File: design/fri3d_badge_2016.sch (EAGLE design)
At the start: 40 parts, among them Q1 MOSFET-NCHANNEL2N7002PW, U1 MCP73831, Y1 8MHz

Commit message: layout tweaks -> v2
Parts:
- removed J1: (no value), SparkFun-Connectors:USB-AB
- removed J2: (no value), SparkFun-Connectors:JST_2MM_MALE
- removed Y1: 8MHz, SparkFun-FreqCtrl:CRYSTALTXC-7A
- added J3: (no value), SparkFun-Connectors:M02JST-PTH-VERT
- added K1: 65100516121, Input-Output_Connectors_rev15d:65100516121
- added Q2: (no value), crystal:CRYSTALHC49S
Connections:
- net GND: now also J3.1, K1.5GND, K1.GND@1, K1.GND@2; no longer J1.GND, J1.SHIELD, J2.-
- net N$1: now also K1.2D-; no longer J1.D-
- net N$2: now also K1.3D+; no longer J1.D+
- net N$8: now also Q2.2; no longer Y1.2
- net N$9: now also Q2.1; no longer Y1.1
- net USBVCC: now also K1.1VCC; no longer J1.VBUS
- net VCC: now also J3.2; no longer J2.+
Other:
- moved on the sheet: R1, R2
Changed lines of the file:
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@@
 </classes>
 <parts>
-<part name="J1" library="SparkFun-Connectors" deviceset="USB-AB" device=""/>
 <part name="FRAME2" library="SparkFun-Aesthetics" deviceset="FRAME-A4L" device=""/>
 <part name="U$1" library="SparkFun-DigitalIC" deviceset="ATMEGA32U4" device="TQFP-44"/>
@@
 <part name="R3" library="SparkFun-Passives" deviceset="RESISTOR" device="0805-RES" value="10K"/>
 <part name="C1" library="SparkFun-Capacitors" deviceset="CAP" device="0805" value="4.7uF"/>
-<part name="J2" library="SparkFun-Connectors" deviceset="JST_2MM_MALE" device=""/>
 <part name="GND3" library="SparkFun-Aesthetics" deviceset="GND" device=""/>
 <part name="GND4" library="SparkFun-Aesthetics" deviceset="GND" device=""/>
@@
 <part name="GND6" library="SparkFun-Aesthetics" deviceset="GND" device=""/>
 <part name="GND7" library="SparkFun-Aesthetics" deviceset="GND" device=""/>
-<part name="Y1" library="SparkFun-FreqCtrl" deviceset="CRYSTAL" device="TXC-7A" value="8MHz"/>
 <part name="C5" library="SparkFun-Capacitors" deviceset="CAP" device="0805" value="18pF"/>
 <part name="C6" library="SparkFun-Capacitors" deviceset="CAP" device="0805" value="18pF"/>
@@
 <part name="LED3" library="led" deviceset="LED" device="CHIPLED_0805"/>
 <part name="LED4" library="led" deviceset="LED" device="CHIPLED_0805"/>
+<part name="Q2" library="crystal" deviceset="CRYSTAL" device="HC49S"/>
+<part name="J3" library="SparkFun-Connectors" deviceset="M02" device="JST-PTH-VERT"/>
+<part name="K1" library="Input-Output_Connectors_rev15d" deviceset="65100516121" device=""/>
 </parts>
 <sheets>
@@
 </plain>
 <instances>
-<instance part="J1" gate="G$1" x="-30.48" y="134.62" rot="R180"/>
 <instance part="FRAME2" gate="G$1" x="-45.72" y="-7.62"/>
 <instance part="U$1" gate="G$1" x="88.9" y="109.22"/>
-<instance part="R1" gate="G$1" x="-5.08" y="132.08"/>
-<instance part="R2" gate="G$1" x="-5.08" y="139.7"/>
-<instance part="GND1" gate="1" x="-20.32" y="121.92"/>
+<instance part="R1" gate="G$1" x="7.62" y="139.7"/>
+<instance part="R2" gate="G$1" x="7.62" y="132.08"/>
+<instance part="GND1" gate="1" x="-7.62" y="142.24"/>
 <instance part="U1" gate="G$1" x="0" y="96.52"/>
 <instance part="GND2" gate="1" x="12.7" y="83.82"/>
 <instance part="R3" gate="G$1" x="17.78" y="91.44" rot="R270"/>
 <instance part="C1" gate="G$1" x="25.4" y="91.44"/>
-<instance part="J2" gate="G$1" x="-5.08" y="63.5" rot="R90"/>
 <instance part="GND3" gate="1" x="5.08" y="58.42"/>
 <instance part="GND4" gate="1" x="-33.02" y="86.36"/>
@@
 <instance part="GND6" gate="1" x="53.34" y="111.76"/>
 <instance part="GND7" gate="1" x="53.34" y="66.04"/>
-<instance part="Y1" gate="G$1" x="63.5" y="96.52" smashed="yes" rot="R90">
-<attribute name="NAME" x="62.484" y="99.06" size="1.778" layer="95" rot="R90"/>
-<attribute name="VALUE" x="66.04" y="99.06" size="1.778" layer="96" rot="R90"/>
-</instance>
 <instance part="C5" gate="G$1" x="55.88" y="101.6" rot="R90"/>
 <instance part="C6" gate="G$1" x="55.88" y="93.98" rot="R90"/>
@@
 <instance part="LED3" gate="G$1" x="205.74" y="40.64" rot="R270"/>
 <instance part="LED4" gate="G$1" x="205.74" y="25.4" rot="R270"/>
+<instance part="Q2" gate="G$1" x="63.5" y="96.52" rot="R90"/>
+<instance part="J3" gate="G$1" x="-10.16" y="63.5"/>
+<instance part="K1" gate="G$1" x="-22.86" y="134.62" rot="R180"/>
 </instances>
 <busses>
@@
 <nets>
 <net name="GND" class="0">
-<segment>
-<pinref part="J1" gate="G$1" pin="GND"/>
-<pinref part="GND1" gate="1" pin="GND"/>
-<wire x1="-25.4" y1="129.54" x2="-20.32" y2="129.54" width="0.1524" layer="91"/>
-<wire x1="-20.32" y1="129.54" x2="-20.32" y2="124.46" width="0.1524" layer="91"/>
-<pinref part="J1" gate="G$1" pin="SHIELD"/>
-<wire x1="-25.4" y1="142.24" x2="-20.32" y2="142.24" width="0.1524" layer="91"/>
-<wire x1="-20.32" y1="142.24" x2="-20.32" y2="129.54" width="0.1524" layer="91"/>
-<junction x="-20.32" y="129.54"/>
-</segment>
 <segment>
 <pinref part="U1" gate="G$1" pin="VSS"/>
@@
 </segment>
 <segment>
-<pinref part="J2" gate="G$1" pin="-"/>
 <pinref part="GND3" gate="1" pin="GND"/>
-<wire x1="0" y1="63.5" x2="5.08" y2="63.5" width="0.1524" layer="91"/>
 <wire x1="5.08" y1="63.5" x2="5.08" y2="60.96" width="0.1524" layer="91"/>
+<pinref part="J3" gate="G$1" pin="1"/>
+<wire x1="5.08" y1="63.5" x2="-2.54" y2="63.5" width="0.1524" layer="91"/>
 </segment>
 <segment>
@@
 <wire x1="152.4" y1="71.12" x2="157.48" y2="71.12" width="0.1524" layer="91"/>
 </segment>
-</net>
-<net name="N$2" class="0">
-<segment>
-<pinref part="J1" gate="G$1" pin="D+"/>
-<pinref part="R1" gate="G$1" pin="1"/>
-<wire x1="-25.4" y1="134.62" x2="-10.16" y2="134.62" width="0.1524" layer="91"/>
-<wire x1="-10.16" y1="134.62" x2="-10.16" y2="132.08" width="0.1524" layer="91"/>
+<segment>
+<pinref part="K1" gate="G$1" pin="5GND"/>
+<wire x1="-15.24" y1="139.7" x2="-15.24" y2="144.78" width="0.1524" layer="91"/>
+<wire x1="-15.24" y1="144.78" x2="-15.24" y2="147.32" width="0.1524" layer="91"/>
+<wire x1="-15.24" y1="147.32" x2="-7.62" y2="147.32" width="0.1524" layer="91"/>
+<pinref part="GND1" gate="1" pin="GND"/>
+<wire x1="-7.62" y1="147.32" x2="-7.62" y2="144.78" width="0.1524" layer="91"/>
+<pinref part="K1" gate="G$1" pin="GND@1"/>
+<wire x1="-17.78" y1="144.78" x2="-15.24" y2="144.78" width="0.1524" layer="91"/>
+<junction x="-15.24" y="144.78"/>
+<pinref part="K1" gate="G$1" pin="GND@2"/>
+<wire x1="-17.78" y1="147.32" x2="-15.24" y2="147.32" width="0.1524" layer="91"/>
+<junction x="-15.24" y="147.32"/>
 </segment>
 </net>
@@
 <segment>
 <pinref part="R1" gate="G$1" pin="2"/>
-<wire x1="0" y1="132.08" x2="7.62" y2="132.08" width="0.1524" layer="91"/>
-<label x="5.08" y="132.08" size="1.778" layer="95"/>
+<wire x1="12.7" y1="139.7" x2="20.32" y2="139.7" width="0.1524" layer="91"/>
+<label x="17.78" y="139.7" size="1.778" layer="95"/>
 </segment>
 <segment>
@@
 <segment>
 <pinref part="R2" gate="G$1" pin="2"/>
-<wire x1="0" y1="139.7" x2="7.62" y2="139.7" width="0.1524" layer="91"/>
-<label x="5.08" y="139.7" size="1.778" layer="95"/>
+<wire x1="12.7" y1="132.08" x2="20.32" y2="132.08" width="0.1524" layer="91"/>
+<label x="17.78" y="132.08" size="1.778" layer="95"/>
 </segment>
 <segment>
@@
 <wire x1="66.04" y1="109.22" x2="66.04" y2="106.68" width="0.1524" layer="91"/>
 <label x="66.04" y="106.68" size="1.778" layer="95"/>
-</segment>
-</net>
-<net name="N$1" class="0">
-<segment>
-<pinref part="J1" gate="G$1" pin="D-"/>
-<pinref part="R2" gate="G$1" pin="1"/>
-<wire x1="-25.4" y1="137.16" x2="-10.16" y2="137.16" width="0.1524" layer="91"/>
-<wire x1="-10.16" y1="137.16" x2="-10.16" y2="139.7" width="0.1524" layer="91"/>
 </segment>
 </net>
@@
 <segment>
 <pinref part="U$1" gate="G$1" pin="VBUS"/>
-<wire x1="71.12" y1="121.92" x2="66.04" y2="121.92" width="0.1524" layer="91"/>
+<label x="53.34" y="121.92" size="1.778" layer="95"/>
 <pinref part="U$1" gate="G$1" pin="UVCC"/>
-<wire x1="66.04" y1="121.92" x2="53.34" y2="121.92" width="0.1524" layer="91"/>
-<wire x1="71.12" y1="119.38" x2="66.04" y2="119.38" width="0.1524" layer="91"/>
-<wire x1="66.04" y1="119.38" x2="66.04" y2="121.92" width="0.1524" layer="91"/>
-<junction x="66.04" y="121.92"/>
-<label x="53.34" y="121.92" size="1.778" layer="95"/>
-</segment>
-<segment>
-<pinref part="J1" gate="G$1" pin="VBUS"/>
-<wire x1="-25.4" y1="139.7" x2="-12.7" y2="139.7" width="0.1524" layer="91"/>
-<wire x1="-12.7" y1="139.7" x2="-12.7" y2="144.78" width="0.1524" layer="91"/>
-<wire x1="-12.7" y1="144.78" x2="7.62" y2="144.78" width="0.1524" layer="91"/>
-<label x="-2.54" y="144.78" size="1.778" layer="95"/>
+<wire x1="68.58" y1="121.92" x2="53.34" y2="121.92" width="0.1524" layer="91"/>
+<wire x1="71.12" y1="119.38" x2="71.12" y2="121.92" width="0.1524" layer="91"/>
+<wire x1="71.12" y1="121.92" x2="68.58" y2="121.92" width="0.1524" layer="91"/>
+</segment>
+<segment>
+<wire x1="0" y1="124.46" x2="20.32" y2="124.46" width="0.1524" layer="91"/>
+<label x="10.16" y="124.46" size="1.778" layer="95"/>
+<wire x1="0" y1="124.46" x2="0" y2="129.54" width="0.1524" layer="91"/>
+<pinref part="K1" gate="G$1" pin="1VCC"/>
+<wire x1="-15.24" y1="129.54" x2="0" y2="129.54" width="0.1524" layer="91"/>
 </segment>
 </net>
@@
 </segment>
 <segment>
-<pinref part="J2" gate="G$1" pin="+"/>
-<wire x1="0" y1="66.04" x2="5.08" y2="66.04" width="0.1524" layer="91"/>
 <label x="0" y="66.04" size="1.778" layer="95"/>
+<pinref part="J3" gate="G$1" pin="2"/>
+<wire x1="5.08" y1="66.04" x2="-2.54" y2="66.04" width="0.1524" layer="91"/>
 </segment>
 <segment>
@@
 <segment>
 <pinref part="U$1" gate="G$1" pin="XTAL1"/>
-<pinref part="Y1" gate="G$1" pin="2"/>
 <wire x1="71.12" y1="99.06" x2="63.5" y2="99.06" width="0.1524" layer="91"/>
 <pinref part="C5" gate="G$1" pin="2"/>
 <wire x1="63.5" y1="99.06" x2="63.5" y2="101.6" width="0.1524" layer="91"/>
 <wire x1="63.5" y1="101.6" x2="58.42" y2="101.6" width="0.1524" layer="91"/>
+<pinref part="Q2" gate="G$1" pin="2"/>
 <junction x="63.5" y="99.06"/>
 </segment>
@@
 <segment>
 <pinref part="U$1" gate="G$1" pin="XTAL2"/>
-<pinref part="Y1" gate="G$1" pin="1"/>
 <wire x1="71.12" y1="93.98" x2="63.5" y2="93.98" width="0.1524" layer="91"/>
 <pinref part="C6" gate="G$1" pin="2"/>
+<pinref part="Q2" gate="G$1" pin="1"/>
 <wire x1="63.5" y1="93.98" x2="58.42" y2="93.98" width="0.1524" layer="91"/>
 <junction x="63.5" y="93.98"/>
@@
 </segment>
 </net>
+<net name="N$1" class="0">
+<segment>
+<pinref part="R2" gate="G$1" pin="1"/>
+<pinref part="K1" gate="G$1" pin="2D-"/>
+<wire x1="2.54" y1="132.08" x2="-15.24" y2="132.08" width="0.1524" layer="91"/>
+</segment>
+</net>
+<net name="N$2" class="0">
+<segment>
+<pinref part="R1" gate="G$1" pin="1"/>
+<wire x1="2.54" y1="139.7" x2="0" y2="139.7" width="0.1524" layer="91"/>
+<wire x1="0" y1="139.7" x2="0" y2="134.62" width="0.1524" layer="91"/>
+<pinref part="K1" gate="G$1" pin="3D+"/>
+<wire x1="0" y1="134.62" x2="-15.24" y2="134.62" width="0.1524" layer="91"/>
+</segment>
+</net>

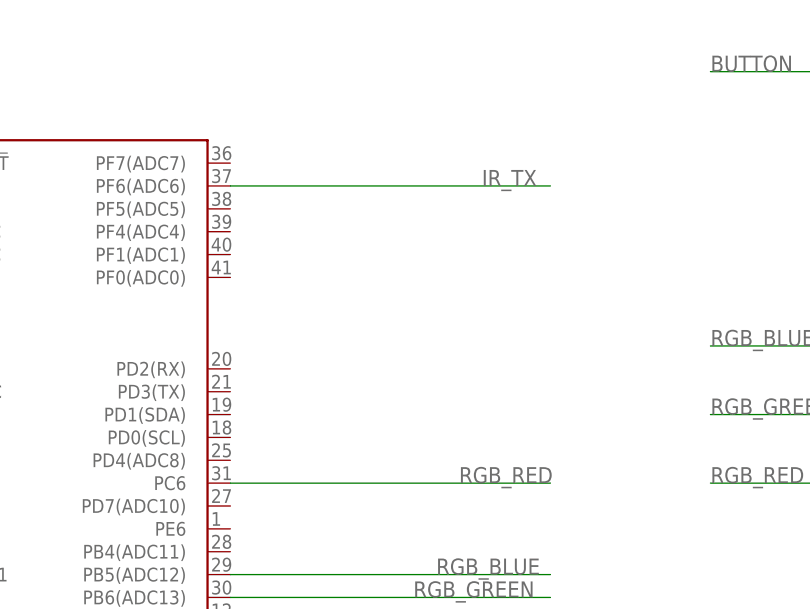
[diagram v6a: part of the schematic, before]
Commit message: fixed wrongly connected IR LED net
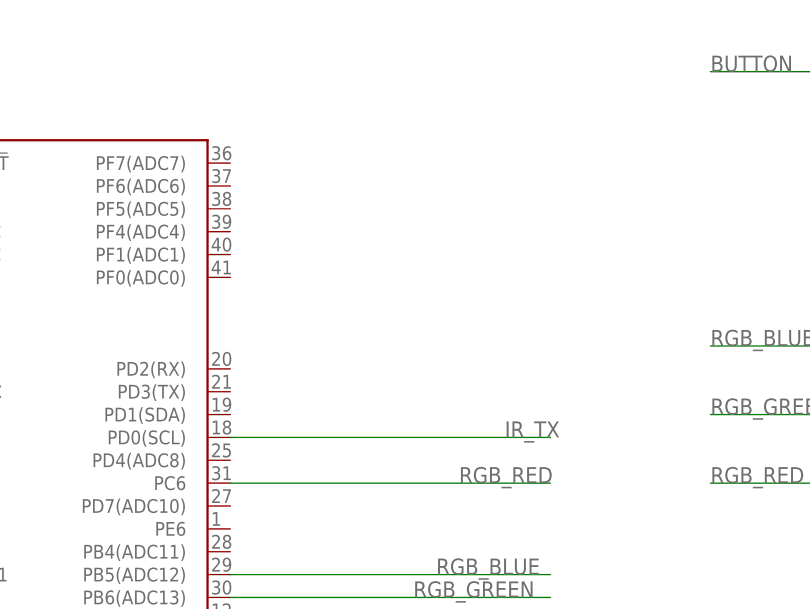
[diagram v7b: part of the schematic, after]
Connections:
- net IR_TX: now also U$1.PD0(SCL); no longer U$1.PF6(ADC6)
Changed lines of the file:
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@@
 </segment>
 <segment>
-<pinref part="U$1" gate="G$1" pin="PF6(ADC6)"/>
-<wire x1="106.68" y1="142.24" x2="142.24" y2="142.24" width="0.1524" layer="91"/>
-<label x="134.62" y="142.24" size="1.778" layer="95"/>
+<pinref part="U$1" gate="G$1" pin="PD0(SCL)"/>
+<wire x1="106.68" y1="114.3" x2="142.24" y2="114.3" width="0.1524" layer="91"/>
+<label x="137.16" y="114.3" size="1.778" layer="95"/>
 </segment>
 </net>
